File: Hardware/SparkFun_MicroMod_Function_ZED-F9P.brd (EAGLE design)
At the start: 38 x 65 mm, 112 parts, among them J1 USB Female Type C Connector, J10 U.FL, J11 455-1750-1-ND, J15 QWIIC_VERT, J16 QWIIC_RA, J18 Bus Selection, J2 MICROMOD_STANDARD, J3 Bus Selection, Q1 DMP21D0UT, U1 SN74LVC1G66DRYR, U10 SN74AUP1T04DCK, U11 SN74AUP1T04DCK, U2 3.3V, U3 EEPROM, U4 74LVC4066D_QUAD_BILATERAL_SWI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, U5 74LVC4066D_QUAD_BILATERAL_SWI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, U6 OPA344, U7 74LVC541ABQ, U8 U-BLOX_ZED-F9P, U9 FIN1017MXSOIC-8

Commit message: End of Day commit.
Got Buzzard working. Added a couple labels.
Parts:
- added U$34: (no value), output:10
- added U$35: (no value), output:211
- added U$36: (no value), output:3212
- added U$38: (no value), output:43213
- added U$39: (no value), output:#RTCMTX#0
- added U$40: (no value), output:#RTCMRX#0
- added U$41: (no value), output:#GND#0
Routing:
- net ZED_ANT_OFF: track 18.9 -> 17.1 mm
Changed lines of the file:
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@@
 <drawing>
 <settings>
-<setting alwaysvectorfont="no"/>
+<setting alwaysvectorfont="yes"/>
 <setting verticaltext="up"/>
 </settings>
@@
 <layer number="23" name="tOrigins" color="15" fill="1" visible="yes" active="yes"/>
 <layer number="24" name="bOrigins" color="15" fill="1" visible="yes" active="yes"/>
-<layer number="25" name="tNames" color="7" fill="1" visible="yes" active="yes"/>
-<layer number="26" name="bNames" color="7" fill="1" visible="yes" active="yes"/>
-<layer number="27" name="tValues" color="7" fill="1" visible="yes" active="yes"/>
-<layer number="28" name="bValues" color="7" fill="1" visible="yes" active="yes"/>
+<layer number="25" name="tNames" color="7" fill="1" visible="no" active="yes"/>
+<layer number="26" name="bNames" color="7" fill="1" visible="no" active="yes"/>
+<layer number="27" name="tValues" color="7" fill="1" visible="no" active="yes"/>
+<layer number="28" name="bValues" color="7" fill="1" visible="no" active="yes"/>
 <layer number="29" name="tStop" color="7" fill="3" visible="yes" active="yes"/>
 <layer number="30" name="bStop" color="7" fill="6" visible="yes" active="yes"/>
@@
 <groups>
 <board_group name="L2_GND_PLANE"/>
-<board_group name="L3_3V3_PLANE"/>
-<board_group name="L4_GND_PLANE"/>
+<board_group name="L15_GND_PLANE"/>
+<board_group name="L16_GND_PLANE"/>
 <board_group name="L1_GND_PLANE"/>
 <board_group name="L1_GRF_PLANE"/>
 <board_group name="L2_GRF_PLANE"/>
-<board_group name="L3_VZED_PLANE"/>
+<board_group name="L15_VZED_PLANE"/>
+<board_group name="L16_GRF_PLANE"/>
 </groups>
 <elements>
@@
 <attribute name="VALUE" x="32.59633125" y="17.696" size="0.6096" layer="27" rot="R90"/>
 </element>
+<element name="U$34" library="output" package="10" value="" x="28.8" y="8.7" smashed="yes"/>
+<element name="U$35" library="output" package="211" value="" x="29.3" y="8.7" smashed="yes"/>
+<element name="U$36" library="output" package="3212" value="" x="30" y="8.7" smashed="yes"/>
+<element name="U$38" library="output" package="43213" value="" x="30.8" y="8.7" smashed="yes"/>
+<element name="U$39" library="output" package="#RTCMTX#0" value="" x="34.5" y="10" smashed="yes" rot="MR0"/>
+<element name="U$40" library="output" package="#RTCMRX#0" value="" x="34.5" y="12.6" smashed="yes" rot="MR0"/>
+<element name="U$41" library="output" package="#GND#0" value="" x="34.5" y="7.5" smashed="yes" rot="MR0"/>
 </elements>
 <signals>
@@
 <via x="34" y="64.5" extent="1-16" drill="0.2"/>
 <via x="30.6" y="62.8" extent="1-16" drill="0.2"/>
-<polygon width="0.25" layer="16" thermals="no">
+<polygon width="0.25" layer="16" thermals="no" grouprefs="L16_GND_PLANE">
 <vertex x="12.4" y="18.2"/>
 <vertex x="14.8" y="18.2"/>
@@
 <vertex x="38.3" y="65.2"/>
 </polygon>
-<polygon width="0.25" layer="16" rank="3">
+<polygon width="0.25" layer="16" rank="3" grouprefs="L16_GND_PLANE">
 <vertex x="-0.1" y="65.2"/>
 <vertex x="-0.1" y="2.6"/>
@@
 <vertex x="38.3" y="65.2"/>
 </polygon>
-<polygon width="0.25" layer="15" thermals="no" rank="3">
+<polygon width="0.25" layer="15" thermals="no" rank="3" grouprefs="L15_GND_PLANE">
 <vertex x="-0.2" y="65.2"/>
 <vertex x="-0.2" y="1.8"/>
@@
 <wire x1="19.55" y1="1.525" x2="19.6" y2="1.575" width="0.2" layer="16"/>
 <wire x1="19.6" y1="1.575" x2="19.6" y2="3.02258125" width="0.2" layer="16"/>
-<wire x1="19.6" y1="3.02258125" x2="21.33061875" y2="4.7532" width="0.2" layer="16"/>
+<wire x1="19.6" y1="3.02258125" x2="21.23061875" y2="4.6532" width="0.2" layer="16"/>
 <via x="23.4" y="4.8657" extent="1-16" drill="0.35"/>
 <wire x1="23.4" y1="4.8657" x2="23.4043" y2="4.87" width="0.2" layer="1"/>
 <wire x1="24.065" y1="4.87" x2="24.395" y2="5.2" width="0.2" layer="1"/>
 <wire x1="24.065" y1="4.87" x2="23.4043" y2="4.87" width="0.2" layer="1"/>
-<wire x1="23.4" y1="4.8657" x2="23.2875" y2="4.7532" width="0.2" layer="16"/>
-<wire x1="23.2875" y1="4.7532" x2="21.33061875" y2="4.7532" width="0.2" layer="16"/>
+<wire x1="23.4" y1="4.8657" x2="23.1875" y2="4.6532" width="0.2" layer="16"/>
+<wire x1="23.1875" y1="4.6532" x2="21.23061875" y2="4.6532" width="0.2" layer="16"/>
 </signal>
 <signal name="A2" class="10">
@@
 <wire x1="9.823" y1="60" x2="9.8" y2="60.023" width="0.2" layer="1"/>
 <via x="9.8" y="61" extent="1-16" drill="0.35"/>
-<polygon width="0.25" layer="15" rank="2" grouprefs="L3_VZED_PLANE">
+<polygon width="0.25" layer="15" rank="2" grouprefs="L15_VZED_PLANE">
 <vertex x="24.7" y="57"/>
 <vertex x="29.1" y="52.6"/>
@@
 <contactref element="Q1" pad="P$3"/>
 <contactref element="J3" pad="2"/>
-<via x="12.25" y="53.25" extent="1-16" drill="0.35"/>
-<wire x1="13.2" y1="52.3" x2="17.8" y2="52.3" width="0.2" layer="16"/>
-<wire x1="13.2" y1="52.3" x2="12.25" y2="53.25" width="0.2" layer="16"/>
+<via x="13.55" y="52.65" extent="1-16" drill="0.35"/>
+<wire x1="13.9" y1="52.3" x2="17.8" y2="52.3" width="0.2" layer="16"/>
+<wire x1="13.9" y1="52.3" x2="13.55" y2="52.65" width="0.2" layer="16"/>
 <via x="17.8" y="52.3" extent="1-16" drill="0.35"/>
 <wire x1="17.8" y1="52.3" x2="17.8" y2="50.8" width="0.2" layer="1"/>
 <wire x1="17.8" y1="50.8" x2="17.75" y2="50.75" width="0.2" layer="1"/>
-<wire x1="5.227" y1="56.34" x2="9.16" y2="56.34" width="0.2" layer="16"/>
-<wire x1="12.25" y1="53.25" x2="9.16" y2="56.34" width="0.2" layer="16"/>
-<wire x1="14.8" y1="52.5" x2="14.8" y2="52.4" width="0.2" layer="1"/>
-<wire x1="14.8" y1="52.4" x2="14.74" y2="52.34" width="0.2" layer="1"/>
-<wire x1="14.74" y1="52.34" x2="13.16" y2="52.34" width="0.2" layer="1"/>
-<wire x1="13.16" y1="52.34" x2="12.25" y2="53.25" width="0.2" layer="1"/>
+<wire x1="5.227" y1="56.34" x2="9.86" y2="56.34" width="0.2" layer="16"/>
+<wire x1="13.55" y1="52.65" x2="9.86" y2="56.34" width="0.2" layer="16"/>
+<wire x1="14.8" y1="52.5" x2="14.65" y2="52.65" width="0.2" layer="1"/>
+<wire x1="14.65" y1="52.65" x2="13.55" y2="52.65" width="0.2" layer="1"/>
 </signal>
 <signal name="ZED_TX_READY" class="11">
@@
 <wire x1="15.55" y1="50.75" x2="15.79" y2="50.99" width="0.35" layer="1"/>
 <wire x1="15.79" y1="52.49" x2="15.8" y2="52.5" width="0.35" layer="1"/>
-<wire x1="15.8" y1="52.5" x2="15.2" y2="53.1" width="0.2" layer="1"/>
+<wire x1="15.8" y1="52.5" x2="15.1" y2="53.2" width="0.2" layer="1"/>
 <wire x1="7.95" y1="54.7" x2="7.5" y2="55.15" width="0.2" layer="1"/>
-<wire x1="15.2" y1="53.1" x2="13.1" y2="53.1" width="0.2" layer="1"/>
-<wire x1="13.1" y1="53.1" x2="11.5" y2="54.7" width="0.2" layer="1"/>
+<wire x1="15.1" y1="53.2" x2="13" y2="53.2" width="0.2" layer="1"/>
+<wire x1="13" y1="53.2" x2="11.5" y2="54.7" width="0.2" layer="1"/>
 <wire x1="11.5" y1="54.7" x2="7.95" y2="54.7" width="0.2" layer="1"/>
 </signal>
@@
 <vertex x="24.7" y="60.7"/>
 </polygon>
-<polygon width="0.25" layer="16" rank="2">
+<polygon width="0.25" layer="16" rank="2" grouprefs="L16_GRF_PLANE">
 <vertex x="24.7" y="57"/>
 <vertex x="29.1" y="52.6"/>
@@
 <via x="19.6" y="33.6" extent="1-16" drill="0.2"/>
 <via x="23.6" y="34.1" extent="1-16" drill="0.2"/>
-<via x="9.9" y="56.8" extent="1-16" drill="0.2"/>
+<via x="9.9" y="56.9" extent="1-16" drill="0.2"/>
 <via x="14.3" y="58.4" extent="1-16" drill="0.2"/>
 <via x="14.3" y="60.3" extent="1-16" drill="0.2"/>

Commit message: Silks complete.
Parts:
- removed LOGO1: SFE_LOGO_NAME_FLAME.1_INCH, SparkFun-Aesthetics:SFE_LOGO_NAME_FLAME_.1
- added U$100, U$66, U$67, U$69, U$96: (no value), output:GRF17
- added U$101, U$102, U$46, U$47, U$55, U$56, U$57, U$58, U$59, U$78, U$79: (no value), output:G2
- added U$103: (no value), output:#I2C#SER#30
- added U$104: (no value), SparkFun-Aesthetics:SFE_LOGO_FLAME_STOP_.1
- added U$105: (no value), output:##RESET##0
- added U$106: (no value), output:HIGH_PRECISION_GNSS26
- added U$107, U$110: (no value), output:EN32
- added U$108, U$109: (no value), output:DIS33
- added U$111: (no value), output:SUP35
- added U$112, U$114: (no value), output:ZED#F9P0
- added U$113: (no value), SparkFun-Aesthetics:QWIIC_5MM
- added U$42, U$43, U$99: (no value), output:#GND#0
- added U$44: (no value), output:#PPS##2252
- added U$45: (no value), output:#PPS##2253
- added U$48: (no value), output:#3
- added U$49: (no value), output:#4
- added U$50: (no value), output:#PPS#2254
- added U$51: (no value), output:PPS0
- added U$52: (no value), output:RTK0
- added U$53: (no value), output:#RTK#2255
- added U$54: (no value), output:#WP#8
- added U$60: (no value), output:#EXTINT#0
- added U$61: (no value), output:#EXTINT#2
- added U$62: (no value), output:#USBPWREN#10
- added U$64: (no value), output:#SHLD#12
- added U$65: (no value), output:##RESET##3
- added U$68: (no value), output:COPI2239
- added U$70: (no value), output:#SPI#30
- added U$71: (no value), output:VBATT18
- added U$72: (no value), output:VZ4
- added U$73, U$89, U$90: (no value), output:VZ19
- added U$74: (no value), output:#ANT_OFF#22
- added U$75: (no value), output:#VZ#5
- added U$76: (no value), output:##SB##9
- added U$77: (no value), output:WITH_RTK_CORRECTIONS28
- added U$80: (no value), output:#SB#29
- added U$81: (no value), output:#DSEL#29
- added U$82: (no value), output:RX231
- added U$83: (no value), output:RX232
- added U$84: (no value), output:TX233
- added U$85: (no value), output:TX2234
- added U$86: (no value), output:PPS2235
- added U$87: (no value), output:SCL2236
- added U$88: (no value), output:SDA2237
- added U$91: (no value), output:CIPO2240
- added U$92: (no value), output:SCK2241
- added U$93: (no value), output:TXR2246
- added U$94: (no value), output:#CS#2245
- added U$95: (no value), output:#DSEL#31
- added U$97: (no value), output:#RX2#2249
- added U$98: (no value), output:#TX2#2249
- moved U$27 18.2 mm to (14.3, 44.3)
- moved U$37 17.5 mm to (14.0, 46.3)
- moved LOGO4 17.5 mm to (14.9, 48.2)
- moved JP5 3.28 mm to (7.05, 5.48)
- moved JP6 2.86 mm to (9.45, 5.48)
- moved JP1 2.33 mm to (33.2, 56.8)
- moved U$26 2.02 mm to (32.6, 49.8)
- moved U$63 2.00 mm to (32.6, 51.6)
- moved TP4 1.82 mm to (15.1, 60.8)
- moved TP11 1.60 mm to (15.0, 7.00)
- moved TP18 1.33 mm to (32.2, 33.9)
- moved U$39 1.30 mm to (35.8, 10.0)
- moved U$40 1.30 mm to (35.8, 12.6)
- moved U$41 1.30 mm to (35.8, 7.50)
- moved TP19 1.24 mm to (35.1, 33.9)
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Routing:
- net N$27: track 2.57 -> 5.91 mm
- net V_USB: track 42.2 -> 44.5 mm
- net N$8: track 2.57 -> 4.51 mm
- net N$16: track 4.69 -> 3.14 mm
- net 3.3V: track 45.9 -> 44.6 mm
- net !RESET!: track 81.2 -> 82.5 mm
- net EXTINT: track 81.8 -> 83.0 mm
- net MM_!CS!: track 31.5 -> 32.6 mm
- net PPS: track 44.0 -> 44.6 mm
- net V_ZED: track 25.7 -> 25.1 mm
- net PPS_DIFF_P: track 3.38 -> 3.88 mm
- net PPS_DIFF_N: track 3.35 -> 3.85 mm
- net GND: vias 89 -> 90

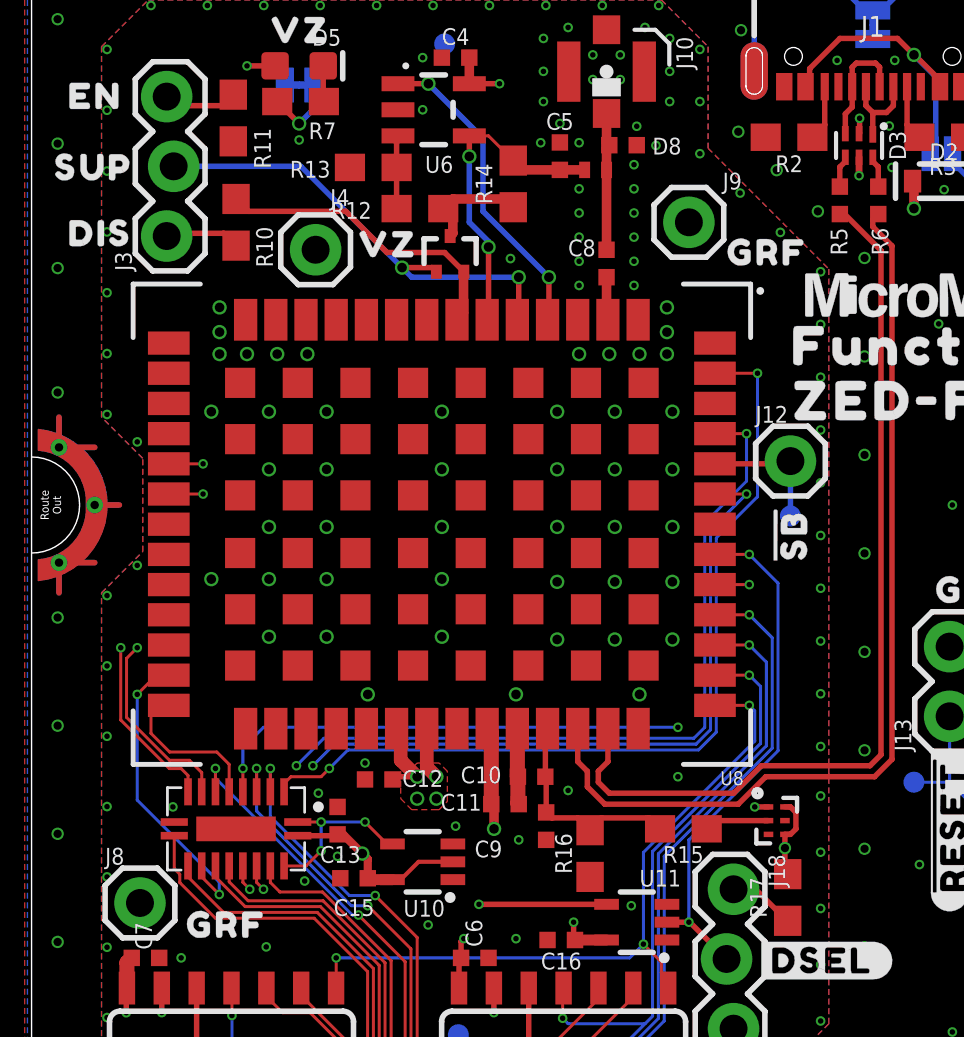
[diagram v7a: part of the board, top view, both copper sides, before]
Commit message: Update New Parts Lib.
Added missing information for new parts to get them ready to be part of normal libraries. Updated schematic and board accordingly.
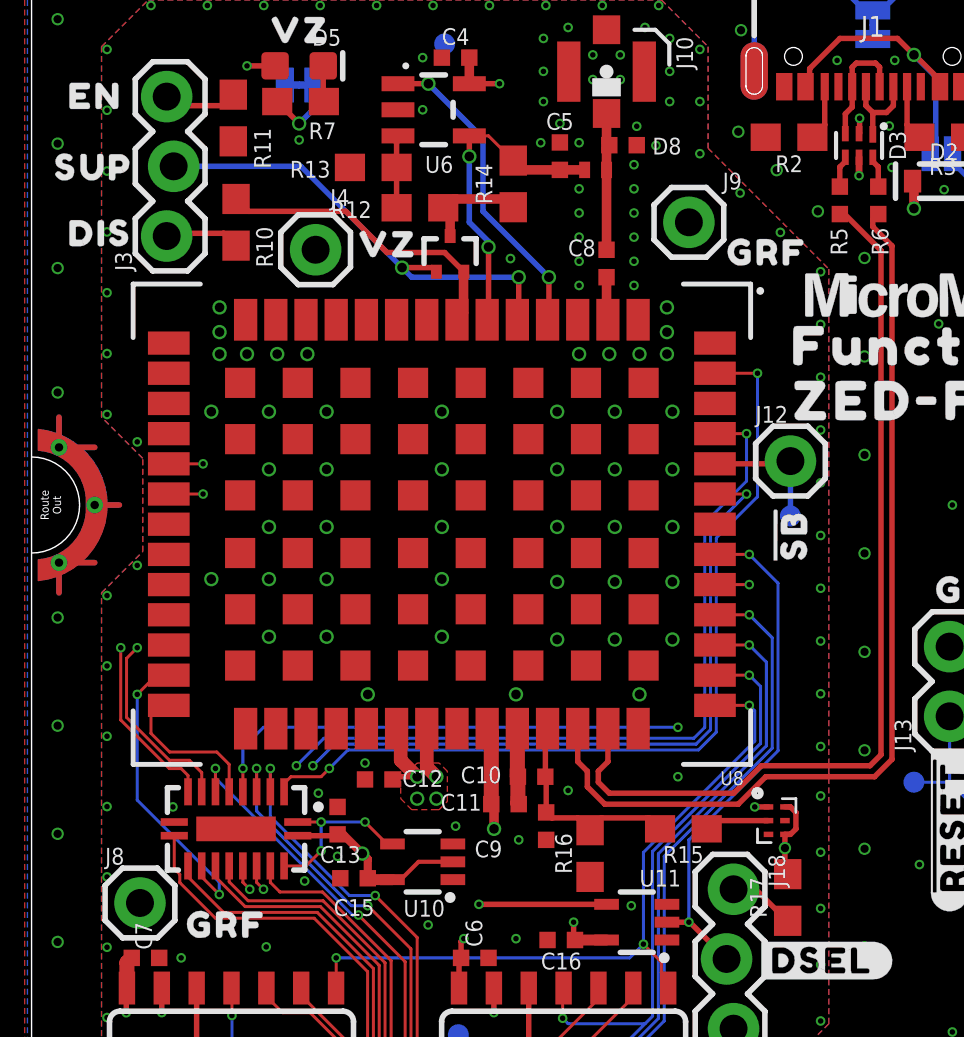
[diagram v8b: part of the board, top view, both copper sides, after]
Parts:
- C8: value CBR04C470J5GAC -> 47pF
- L1: value LQW15AWR15J80D -> 150nH
- Q1: value DMP21D0UT -> DMP21D0UT-7
- U10, U11: value SN74AUP1T04DCK -> SN74AUP1T04
- U7: value 74LVC541ABQ -> 74LVC541A
- U9: value FIN1017MXSOIC-8 -> FIN1017MX
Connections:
- net GND_RF: now also U7.EPAD; no longer U7.P$21
